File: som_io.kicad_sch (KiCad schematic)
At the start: 16 parts, among them J1 Hermaphroditic_Molex_203456-0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, U1 NTS0102_XSON, U2 NTS0102_XSON, U3 NTS0102_XSON, U4 NTS0102_XSON, U5 NTS0102_XSON

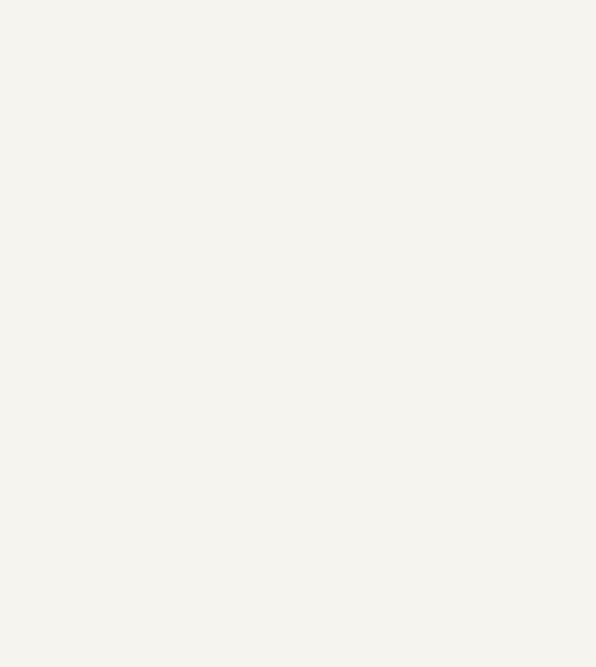
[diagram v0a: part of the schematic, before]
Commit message: [#82847] Prepare current state of schematic to merge with mockup
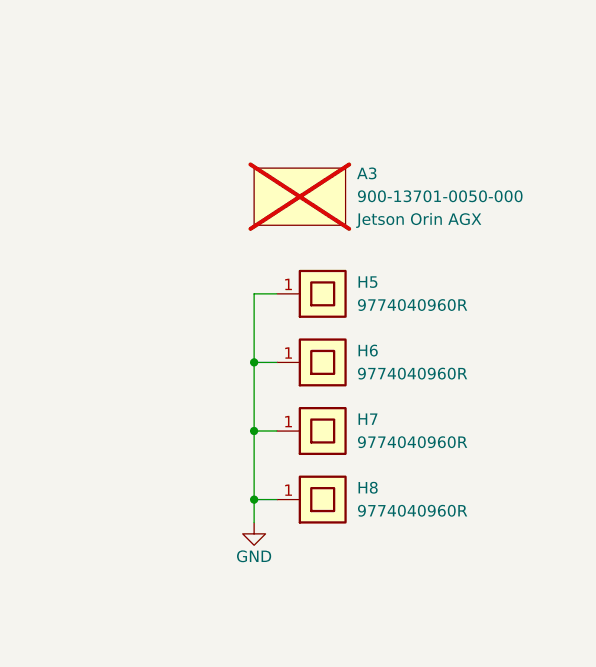
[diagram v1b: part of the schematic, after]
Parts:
- added A3: Jetson-Orin-AGX, antmicro-footprints:Module_Jetson-Orin-AGX, symbol antmicroModules:Jetson-Orin-AGX
- added H5, H6, H7, H8: Spacer_Drill4.45mm_H4mm_9774040960R, antmicro-footprints:Spacer_Drill4.45mm_H4mm_9774040960R, symbol antmicroMechanicalParts:Spacer_Drill4.45mm_H4mm_9774040960R
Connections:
- net GND: now also H5.1, H6.1, H7.1, H8.1

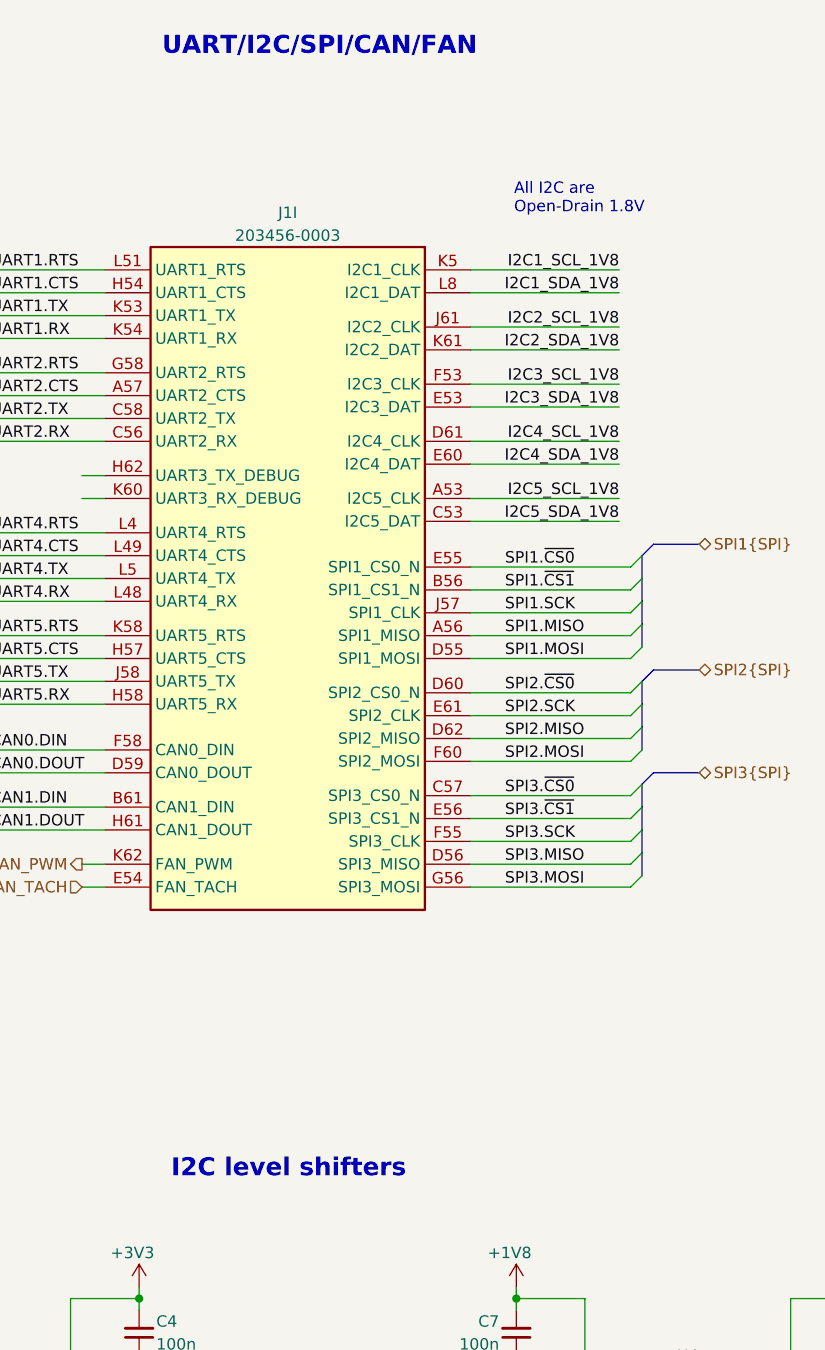
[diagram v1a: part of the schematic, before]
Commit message: [#82837] Standardise sheet sections text size
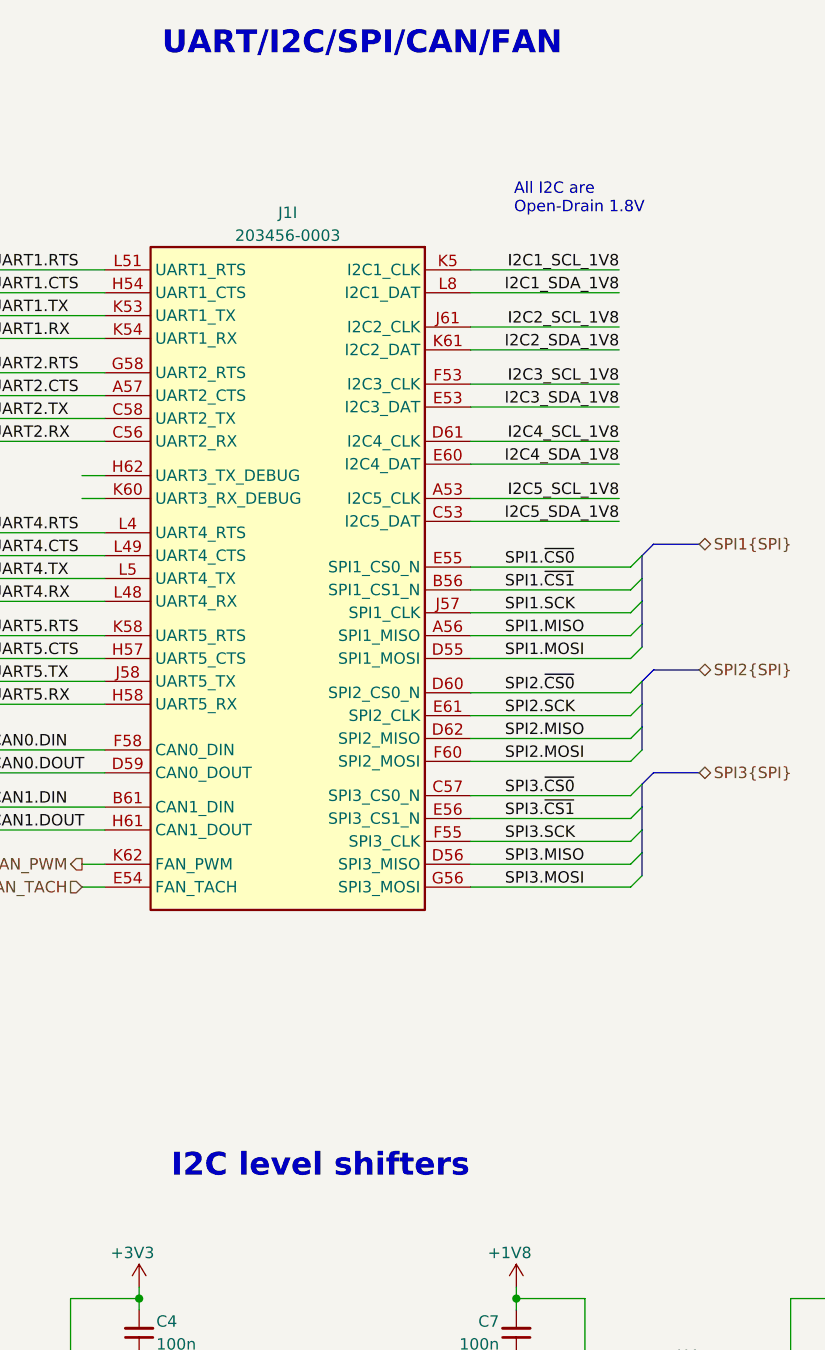
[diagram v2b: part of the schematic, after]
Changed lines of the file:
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@@
 		(effects
 			(font
-				(size 2 2)
+				(size 2.54 2.54)
 				(thickness 0.508)
 				(bold yes)
@@
 		(effects
 			(font
-				(size 2 2)
+				(size 2.54 2.54)
 				(thickness 0.508)
 				(bold yes)

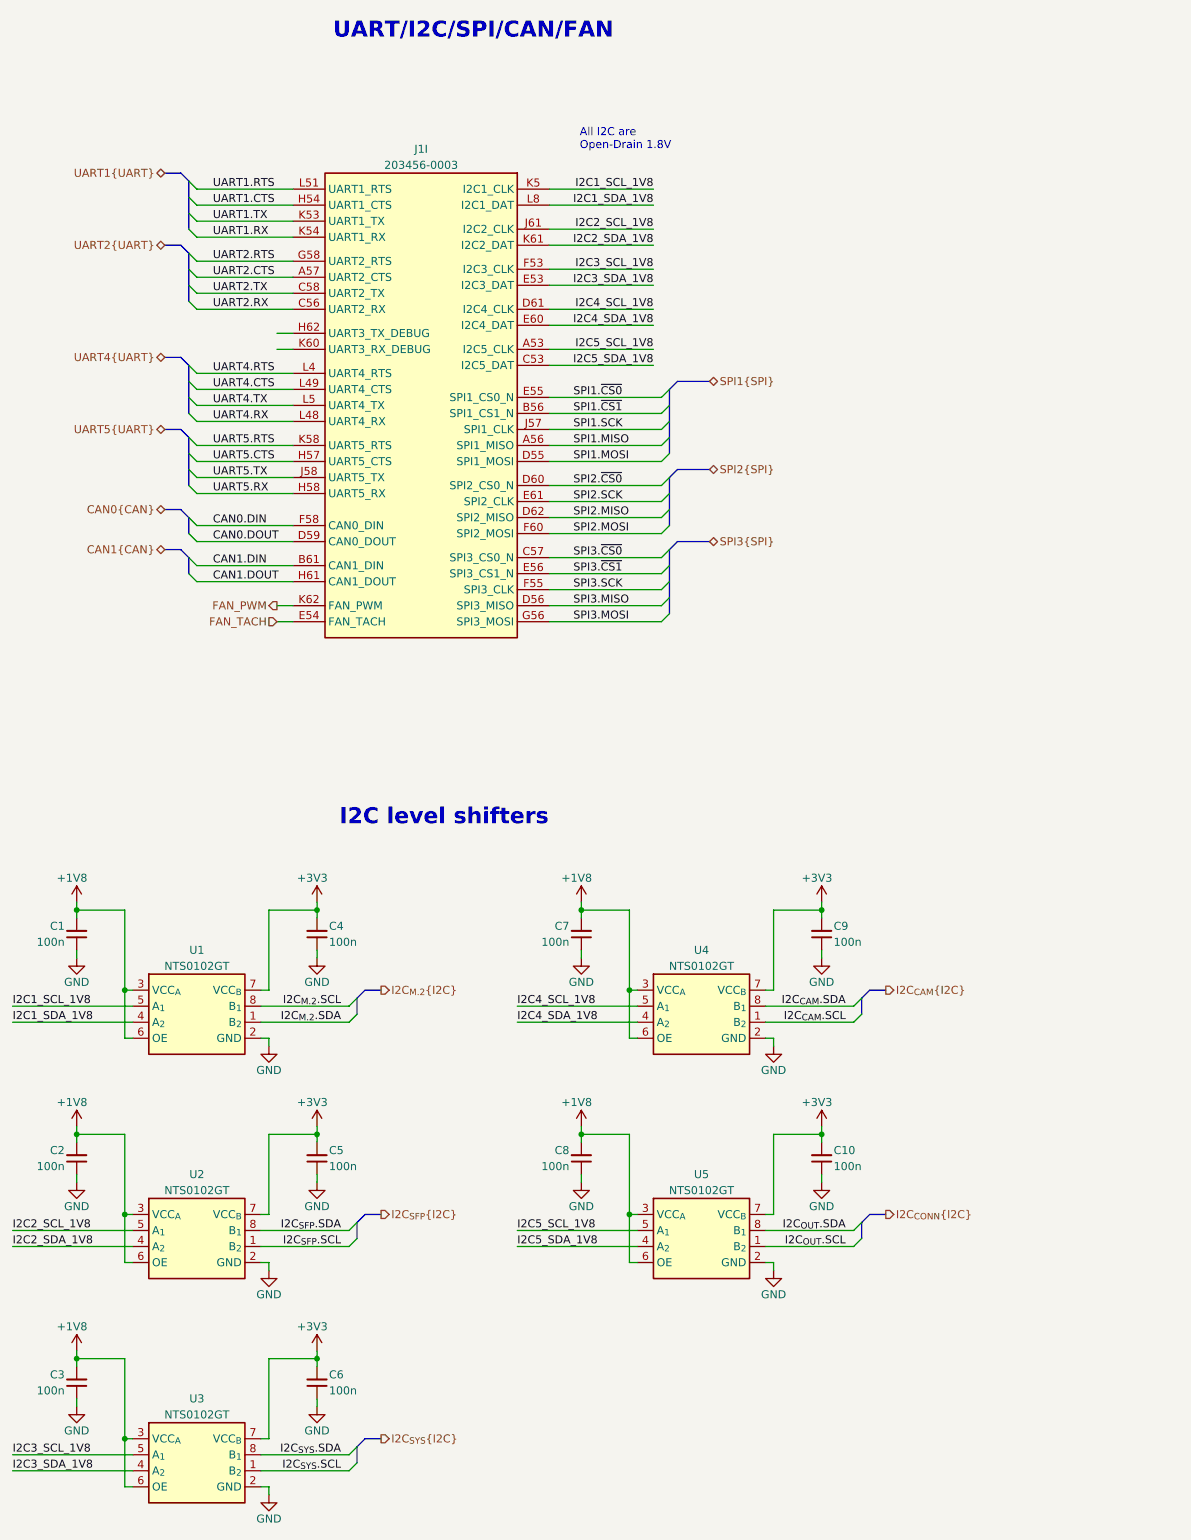
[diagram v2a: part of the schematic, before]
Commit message: [#82837] Finish rerouting USB PD controller, start debug section
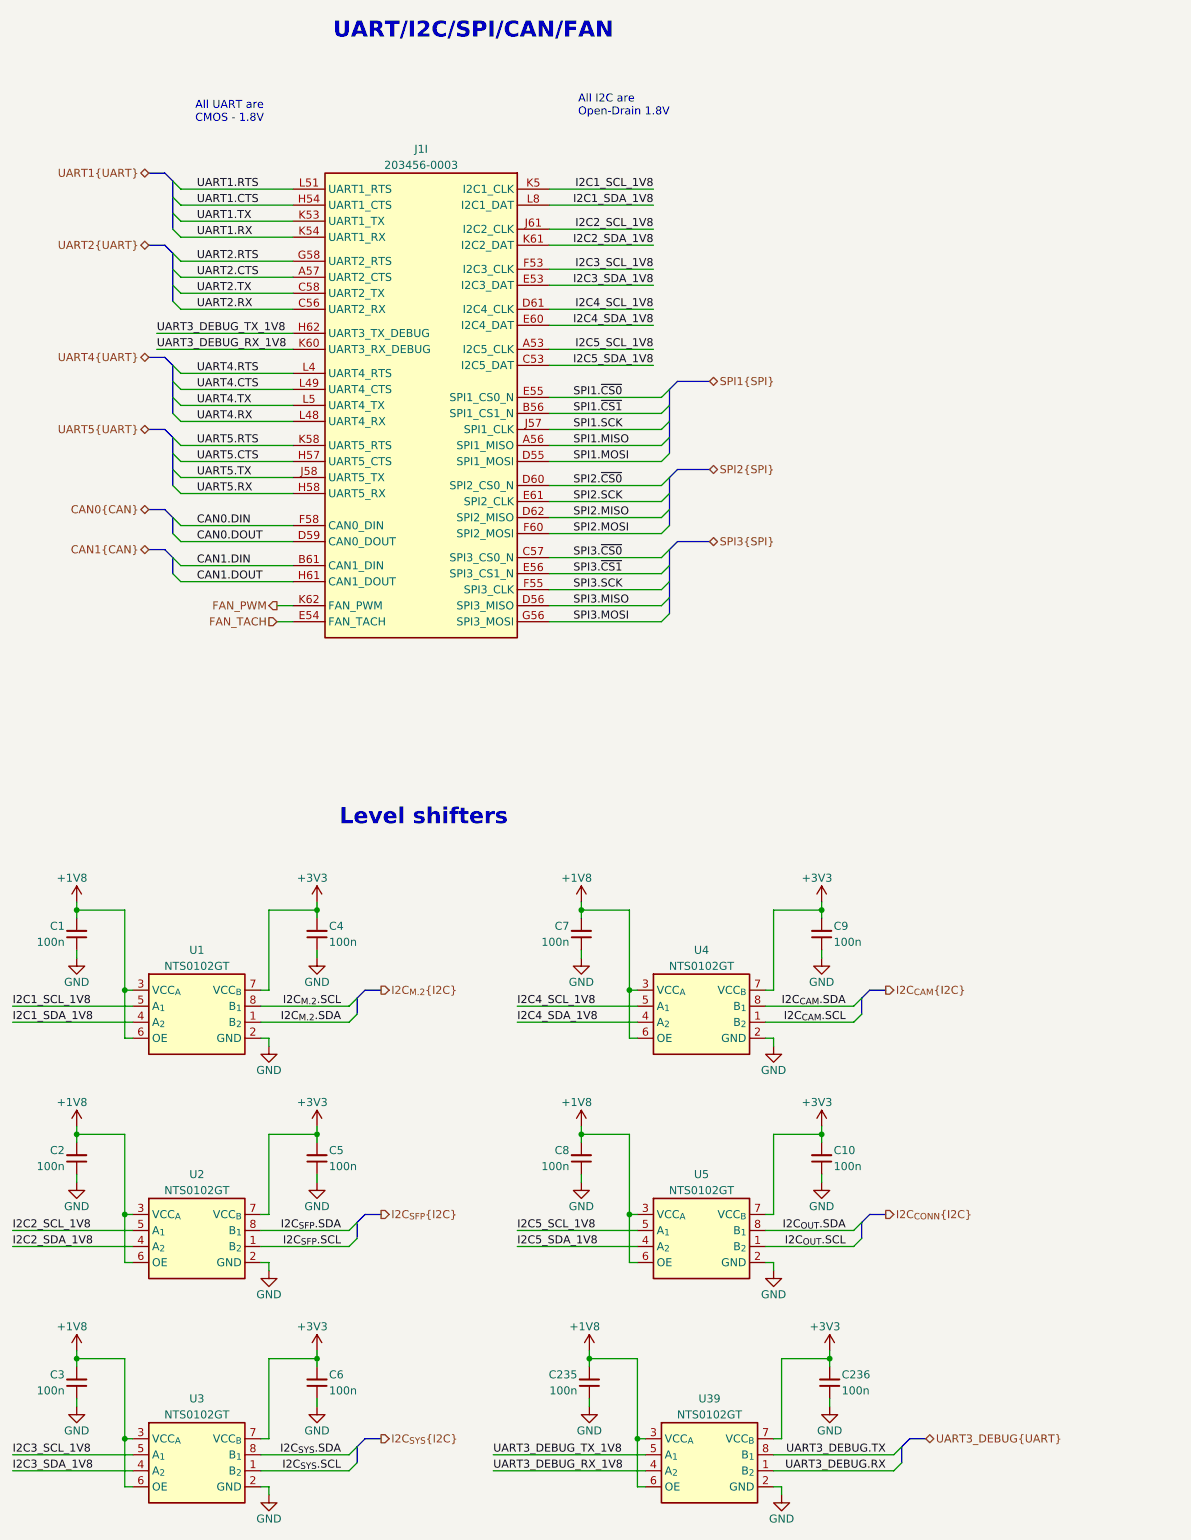
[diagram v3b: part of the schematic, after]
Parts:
- added C235, C236: C_100n_0402, antmicro-footprints:C_0402_1005Metric, symbol antmicroCapacitors0402:C_100n_0402
- added U39: NTS0102_XSON, antmicro-footprints:XSON-8_1x1.95mm_P0.5mm, symbol antmicroLogicTranslatorsLevelShifters:NTS0102_XSON
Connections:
- net +1V8: now also C235.2, U39.3 (VCC_{A}), U39.6 (OE)
- net +3V3: now also C236.2, U39.7 (VCC_{B})
- net GND: now also C235.1, C236.1, U39.2 (GND)
- net UART3_DEBUG_TX_1V8: now reaches J1.H62 (UART3_TX_DEBUG)
- net UART3_DEBUG_TX_1V8: now also U39.5 (A_{1})
- net UART3_DEBUG_RX_1V8: now reaches J1.K60 (UART3_RX_DEBUG)
- net UART3_DEBUG_RX_1V8: now also U39.4 (A_{2})
- new net UART3_DEBUG.RX: U39.1 (B_{2})
- new net UART3_DEBUG.TX: U39.8 (B_{1})
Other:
- note added: "All UART are CMOS - 1.8V"
- note added: "Level shifters"
- note removed: "I2C level shifters"

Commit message: [#82837] Add JTAG debug section to SoM_IO sheet. Delete SoM_Debug sheet and rearrange schematic pages
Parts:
- removed A3: Jetson-Orin-AGX, antmicro-footprints:Module_Jetson-Orin-AGX, symbol antmicroModules:Jetson-Orin-AGX
- removed H5, H6, H7, H8: Spacer_Drill4.45mm_H4mm_9774040960R, antmicro-footprints:Spacer_Drill4.45mm_H4mm_9774040960R, symbol antmicroMechanicalParts:Spacer_Drill4.45mm_H4mm_9774040960R
- added C237, C238: C_100n_50V_X8L_0402, antmicro-footprints:C_0402_1005Metric, symbol antmicroCapacitors0402:C_100n_50V_X8L_0402
- added unit 10 of J1
- added J20: Tag-Connect_TC2050-IDC-NL_2x5_P1.27mm, antmicro-footprints:Tag-Connect_TC2050-IDC-NL_2x5_P1.27mm, symbol antmicroTestPoints:Tag-Connect_TC2050-IDC-NL_2x5_P1.27mm
- added Q28: PJE138K, antmicro-footprints:SOT-523, symbol antmicroTransistorsFETsMOSFETsSingle:PJE138K
- added R126: R_100k_0402, antmicro-footprints:R_0402_1005Metric, symbol antmicroResistors0402:R_100k_0402
- added R285: R_10k_0402, antmicro-footprints:R_0402_1005Metric, symbol antmicroResistors0402:R_10k_0402
- added R290, R291, R292, R293, R294, R295: R_0R_0402, antmicro-footprints:R_0402_1005Metric, symbol antmicroResistors0402:R_0R_0402
- added U59: TXU0304BQAR, antmicro-footprints:DHVQFN-14-1EP_2.5x3mm, symbol antmicroLogicTranslatorsLevelShifters:TXU0304BQAR
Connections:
- net +1V8: now also R290.1, R291.1
- net GND: now also C237.1, C238.1, J20.3, J20.5, J20.9, Q28.2 (S), R126.1, U59.15 (GND), U59.7 (GND)
- new net: C237.2, J20.1, U59.1 (VCCA)
- new net: R295.1, U59.10 (B4)
- new net: R292.1, U59.11 (B3Y)
- new net: R293.1, U59.12 (B2Y)
- new net: R294.1, U59.13 (B1Y)
- new net +1V8_PER: C238.2, R285.2, U59.14 (VCCB), U59.8 (OE)
- new net JTAG_TCK: J1.A60 (JTAG_TCK), R292.2
- new net JTAG_TDI: J1.B60 (JTAG_TDI), R293.2
- new net JTAG_TDO: J1.D58 (JTAG_TDO), R295.2
- new net JTAG_TMS: J1.E58 (JTAG_TMS), R294.2
- new net JTAG_TRST_N: J1.G61 (JTAG_TRST_N), Q28.3 (D), R285.1
- new net NVDBG_SEL: J1.G60 (NVDBG_SEL), R291.2
- new net NVJTAG_SEL: J1.H59 (NVJTAG_SEL), R290.2
- new net TC_JTAG_TCK: J20.4, U59.4 (A3)
- new net TC_JTAG_TDI: J20.8, U59.3 (A2)
- new net TC_JTAG_TDO: J20.6, U59.5 (A4Y)
- new net TC_JTAG_TMS: J20.2, U59.2 (A1)
- new net TC_JTAG_TRST_N: J20.10, Q28.1 (G), R126.2
- no-connect marks 0 -> 1
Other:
- note added: "JTAG DEBUG"
- moved on the sheet: J1G, J1H, J1K

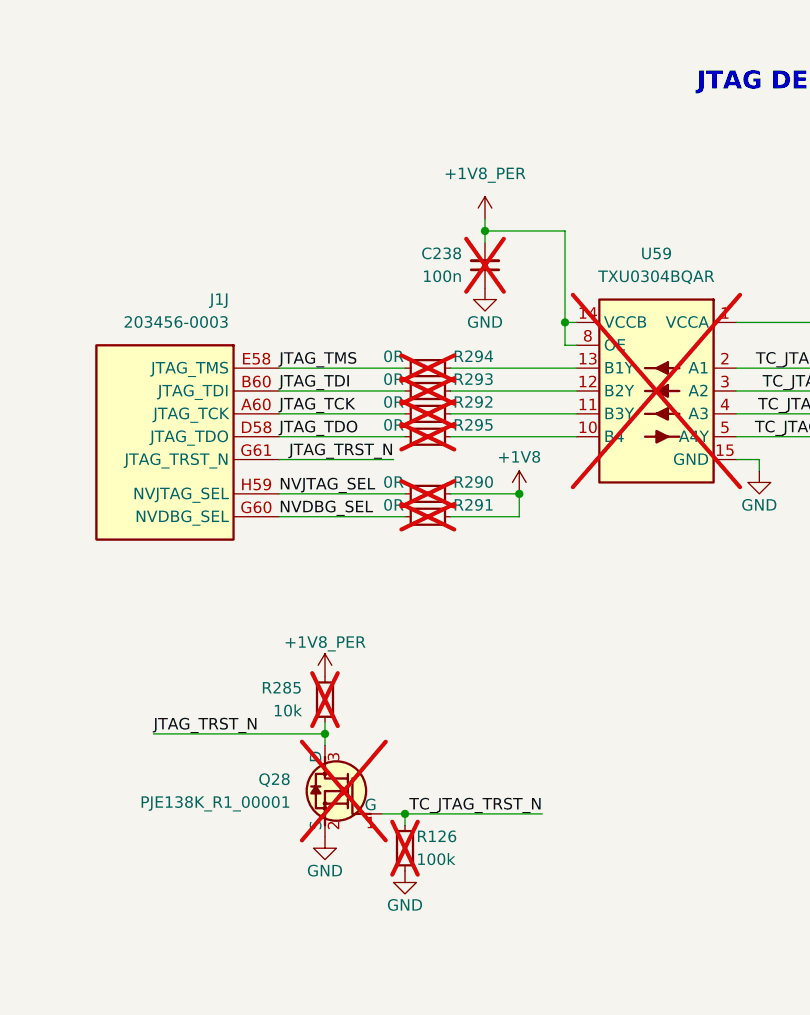
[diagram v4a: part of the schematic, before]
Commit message: [#82837] Prepare schematic to add root connections to USB section
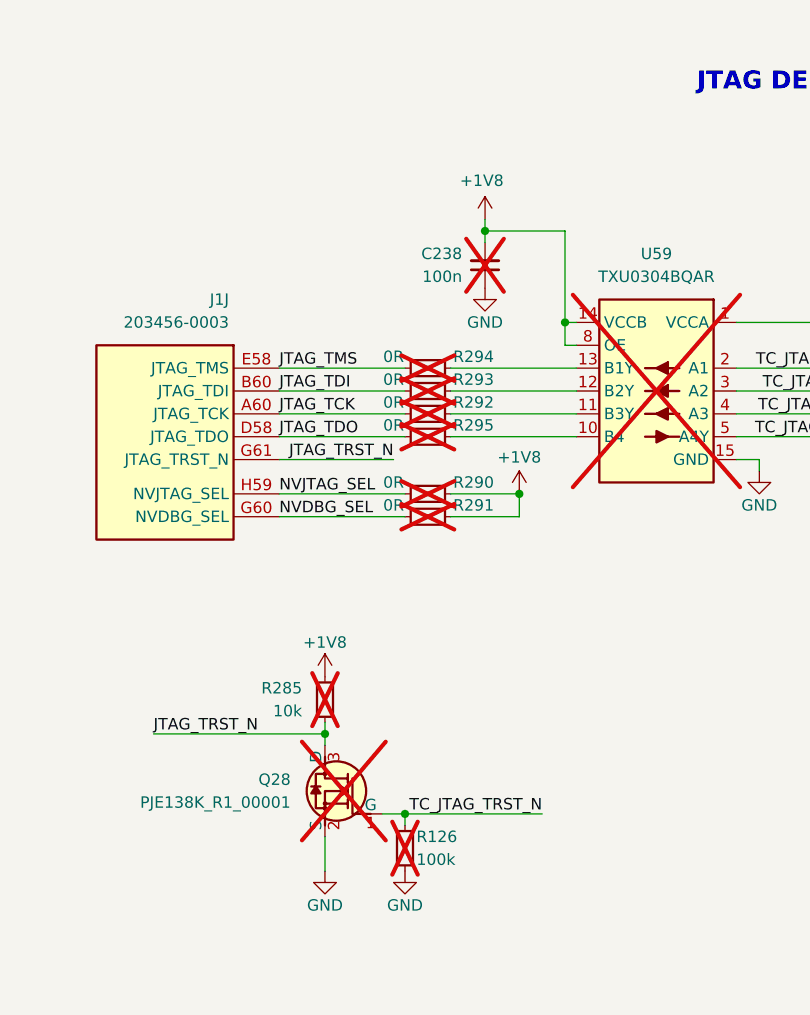
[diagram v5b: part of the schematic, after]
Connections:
- net +1V8_PER is gone; now on net +1V8: C238.2, R285.2, U59.14 (VCCB), U59.8 (OE)
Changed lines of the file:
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@@
 	(wire
 		(pts
+			(xy 262.89 270.51) (xy 262.89 266.7)
+		)
+		(stroke
+			(width 0)
+			(type default)
+		)
+	)
+	(wire
+		(pts
 			(xy 280.67 198.12) (xy 280.67 199.39)
 		)
@@
 		(on_board yes)
 		(dnp no)
-		(fields_autoplaced yes)
 		(property "Reference" "#PWR0504"
 			(at 280.67 201.93 0)
@@
 			)
 		)
-		(property "Value" "+1V8_PER"
-			(at 280.67 193.04 0)
+		(property "Value" "+1V8"
+			(at 277.876 193.802 0)
 			(effects
 				(font
 					(size 1.27 1.27)
 				)
+				(justify right)
 			)
 		)
@@
 	(symbol
 		(lib_id "antmicropower:GND")
-		(at 262.89 266.7 0)
+		(at 262.89 270.51 0)
 		(mirror y)
 		(unit 1)
@@
 		(dnp no)
 		(property "Reference" "#PWR0502"
-			(at 254 269.24 0)
+			(at 254 273.05 0)
 			(effects
 				(font
@@
 		)
 		(property "Value" "GND"
-			(at 262.89 270.51 0)
+			(at 262.89 274.32 0)
 			(effects
 				(font
@@
 		)
 		(property "Footprint" ""
-			(at 254 274.32 0)
+			(at 254 278.13 0)
 			(effects
 				(font
@@
 		)
 		(property "Datasheet" ""
-			(at 254 279.4 0)
+			(at 254 283.21 0)
 			(effects
 				(font
@@
 		)
 		(property "Description" ""
-			(at 262.89 266.7 0)
+			(at 262.89 270.51 0)
 			(effects
 				(font
@@
 		)
 		(property "Author" "Antmicro"
-			(at 254 274.32 0)
+			(at 254 278.13 0)
 			(effects
 				(font
@@
 		)
 		(property "License" "Apache-2.0"
-			(at 254 276.86 0)
+			(at 254 280.67 0)
 			(effects
 				(font
@@
 			)
 		)
-		(property "Value" "+1V8_PER"
+		(property "Value" "+1V8"
 			(at 262.89 245.11 0)
 			(effects
